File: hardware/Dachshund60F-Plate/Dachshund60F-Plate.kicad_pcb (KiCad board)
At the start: 2 copper layers, 318.5 x 134.1 mm, 0 parts

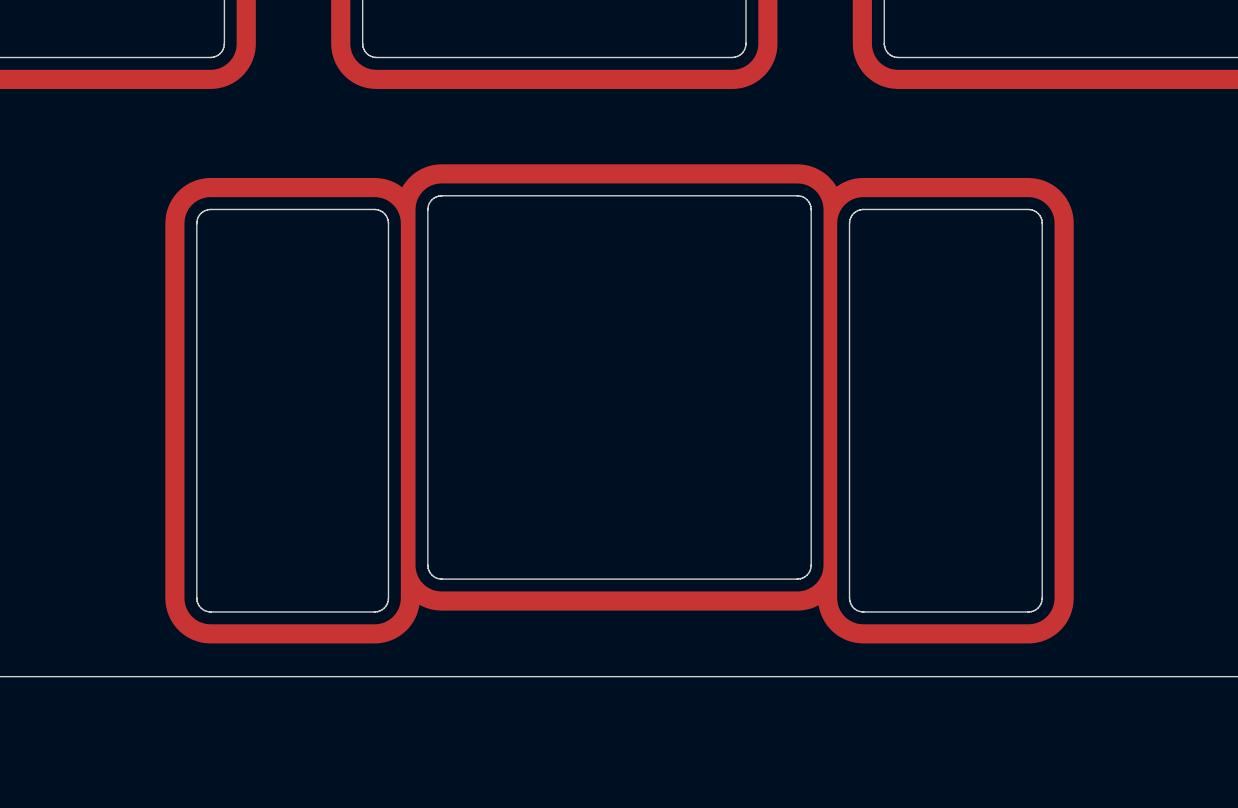
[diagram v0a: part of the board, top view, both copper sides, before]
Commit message: Mainboard: flip the roller encoder so its shaft points right
SW3 moves from (330.3, 47.025) at 0 deg to (314.3, 52.025) at 180 deg: the
body sits just right of the last key column and the shaft points toward the
board edge (tip at x ~331.3), so the wheel can be about 17 mm wide.

Reroute ENC_A, ENC_B, COL14 and ENC_SW to the new pads (one new ENC_A via),
dip ROW0 under the new lower mounting tab, drop the two GND stitching vias
the new pins landed on, move the back-side name/version/JLC text off the
pins and refill the zones. DRC is unchanged: 0 errors, 0 unconnected, 0
parity issues.

Regenerate the plate (the notch is unchanged) and refresh the STEP exports.
The case still has the old roller position; that's a scheduled task.

Co-Authored-By: Claude Opus 5.5 (1M context) <noreply@anthropic.com>
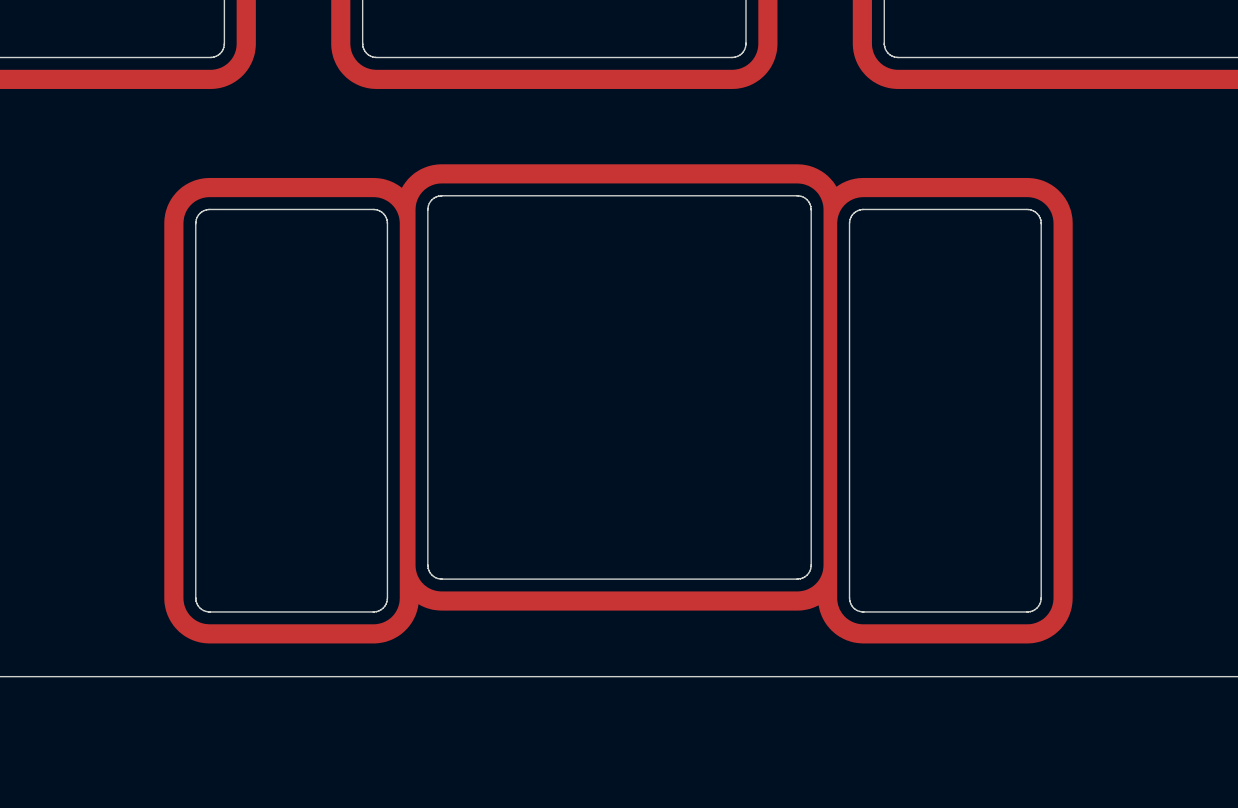
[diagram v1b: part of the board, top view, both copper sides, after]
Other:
- outline, holes or cut-outs redrawn

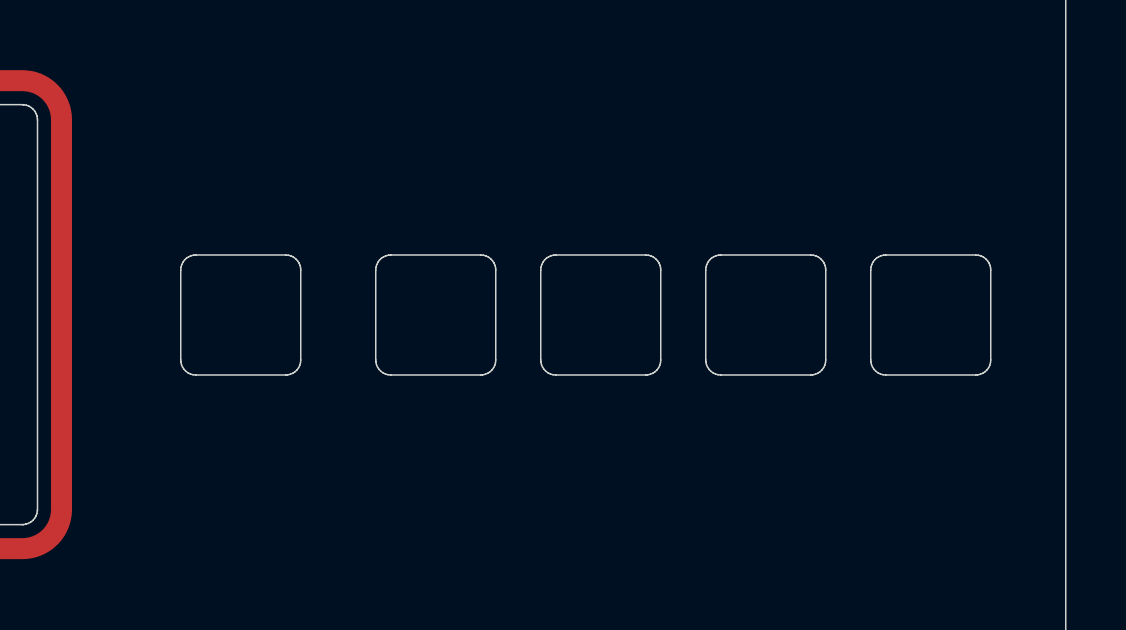
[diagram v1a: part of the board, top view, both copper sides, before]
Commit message: Mainboard: move status LEDs right, wider gap after D3
D3 310.0 -> 310.5, D4-D7 316.5/322/327.5/333 -> 318.5/324/329.5/335 (y 130.5),
with their light cutouts and caps (C14-C18). The gap after the layer LED is
8.0 mm (was 6.5) for the case's notch; the battery LEDs keep their 5.5 mm
pitch. Reroute the data chain and LED supply, drop a stitching via that
D5's pads now straddle, move D7's reference off the edge and refill.
DRC: 0 errors, 0 unconnected, 0 parity issues; warnings unchanged.

Regenerate the plate's LED windows, refresh the STEP exports and move the
indicator positions in keyboard.json.

Co-Authored-By: Claude Opus 5.5 (1M context) <noreply@anthropic.com>
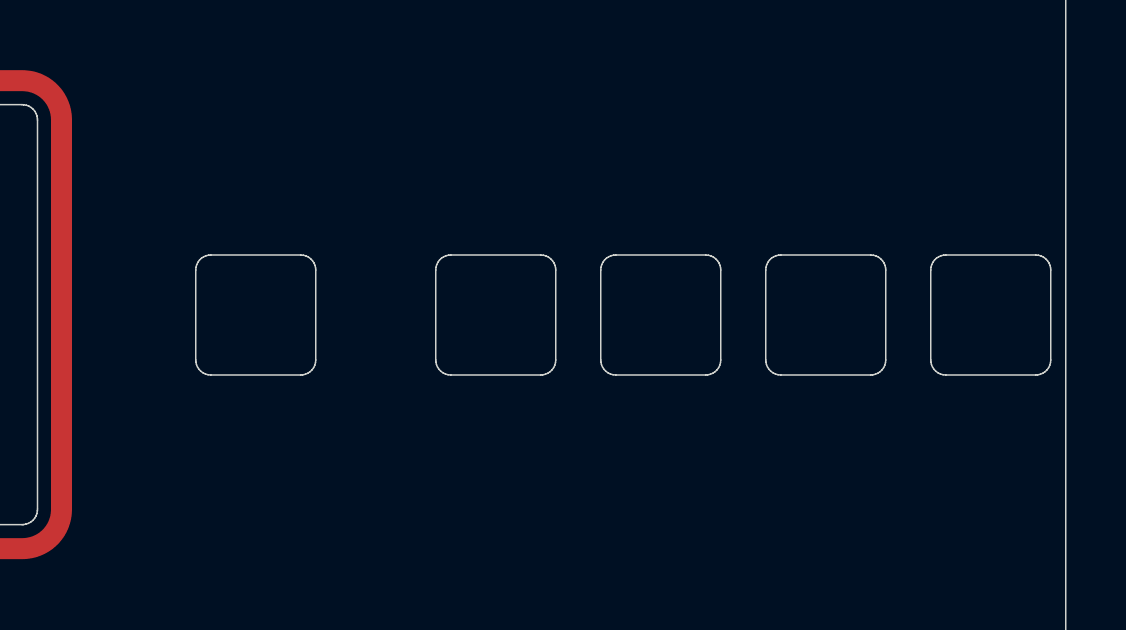
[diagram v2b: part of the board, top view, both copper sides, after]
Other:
- outline, holes or cut-outs redrawn
